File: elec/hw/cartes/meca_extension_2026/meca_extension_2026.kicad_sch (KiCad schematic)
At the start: 101 parts, among them J1 2-1445051-3, J14 22272031, J15 22272031, J16 5264-3P, J26 22053051, J27 22053041, Q19 BSS84, Q20 2N7002, U1 TCA9548APWR, U11 LV14340DDAR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

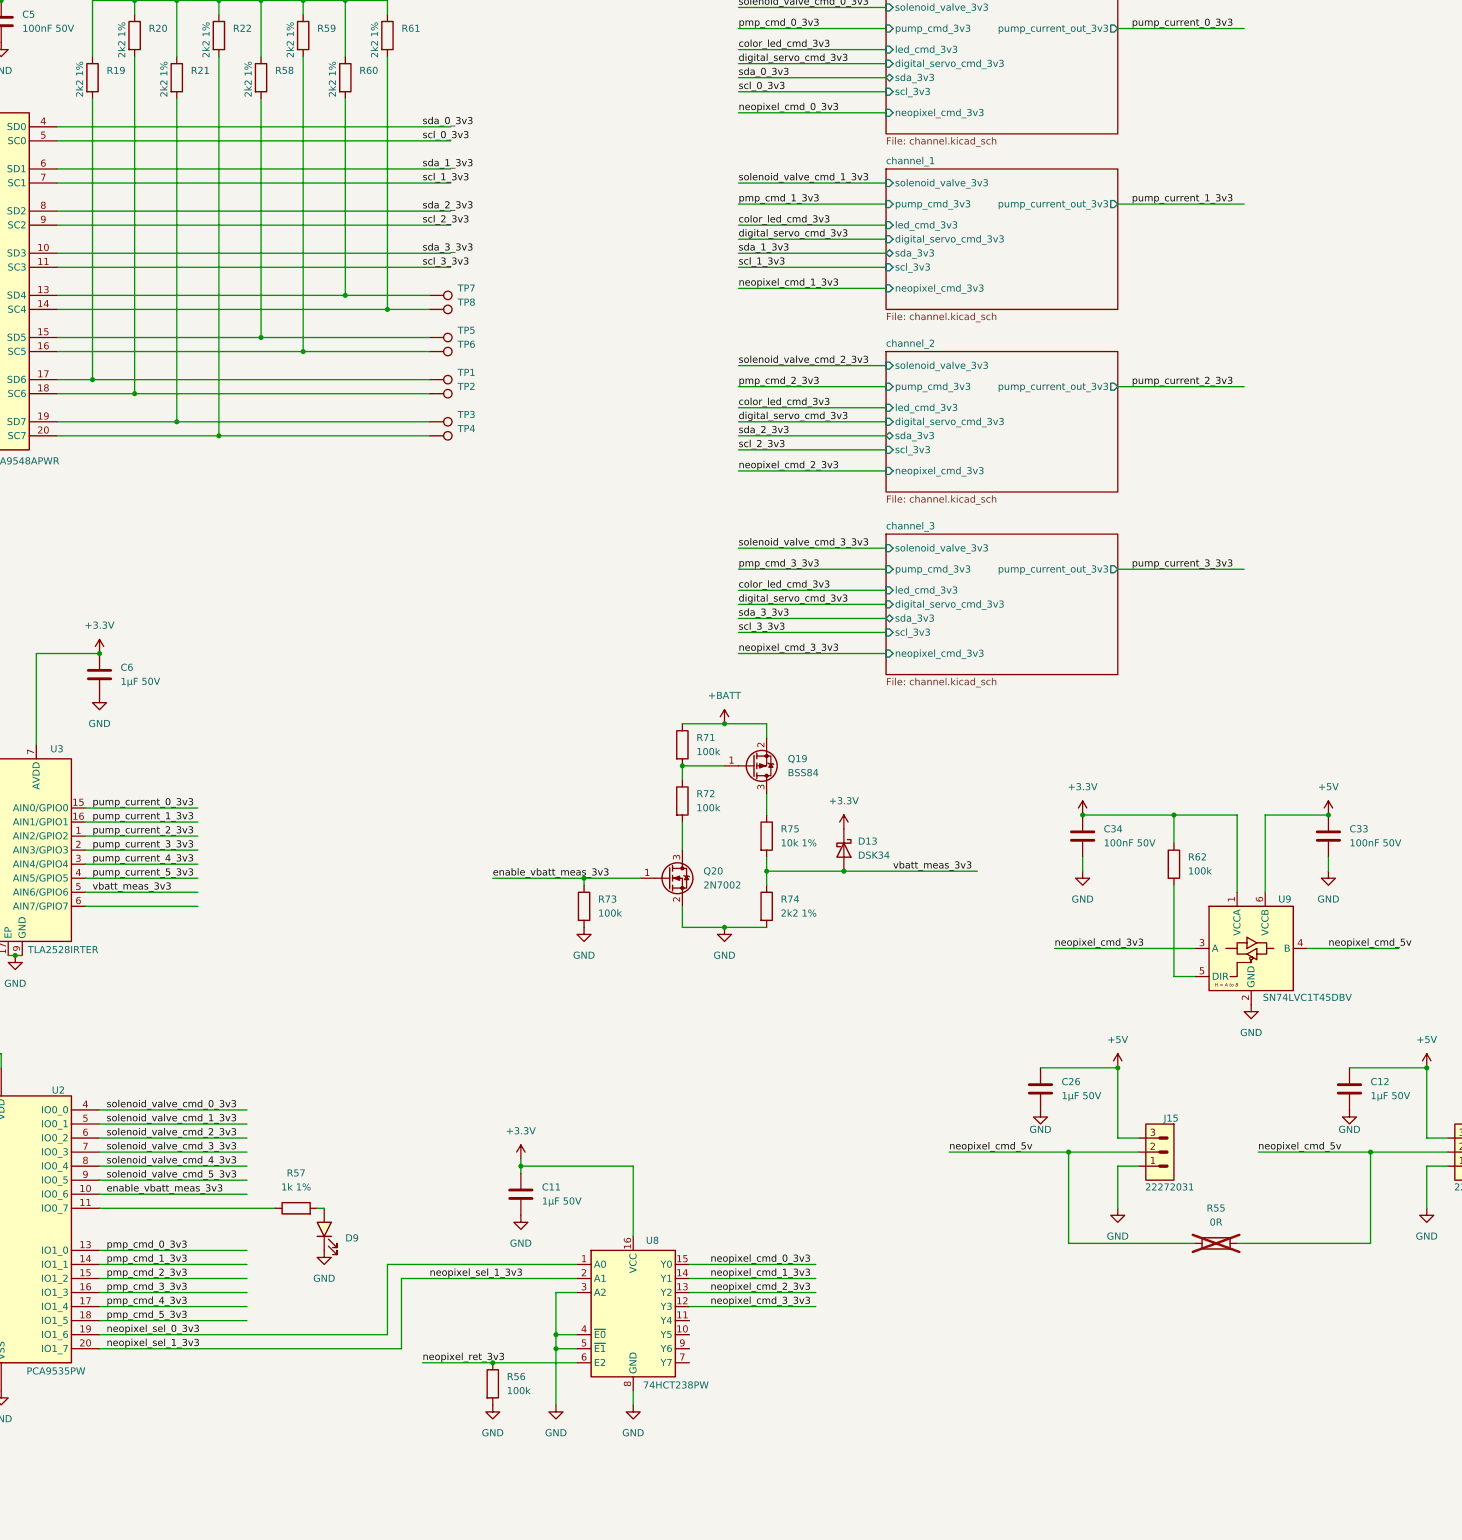
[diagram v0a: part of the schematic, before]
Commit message: meca_extension : schematic correction and routing modified accordingly
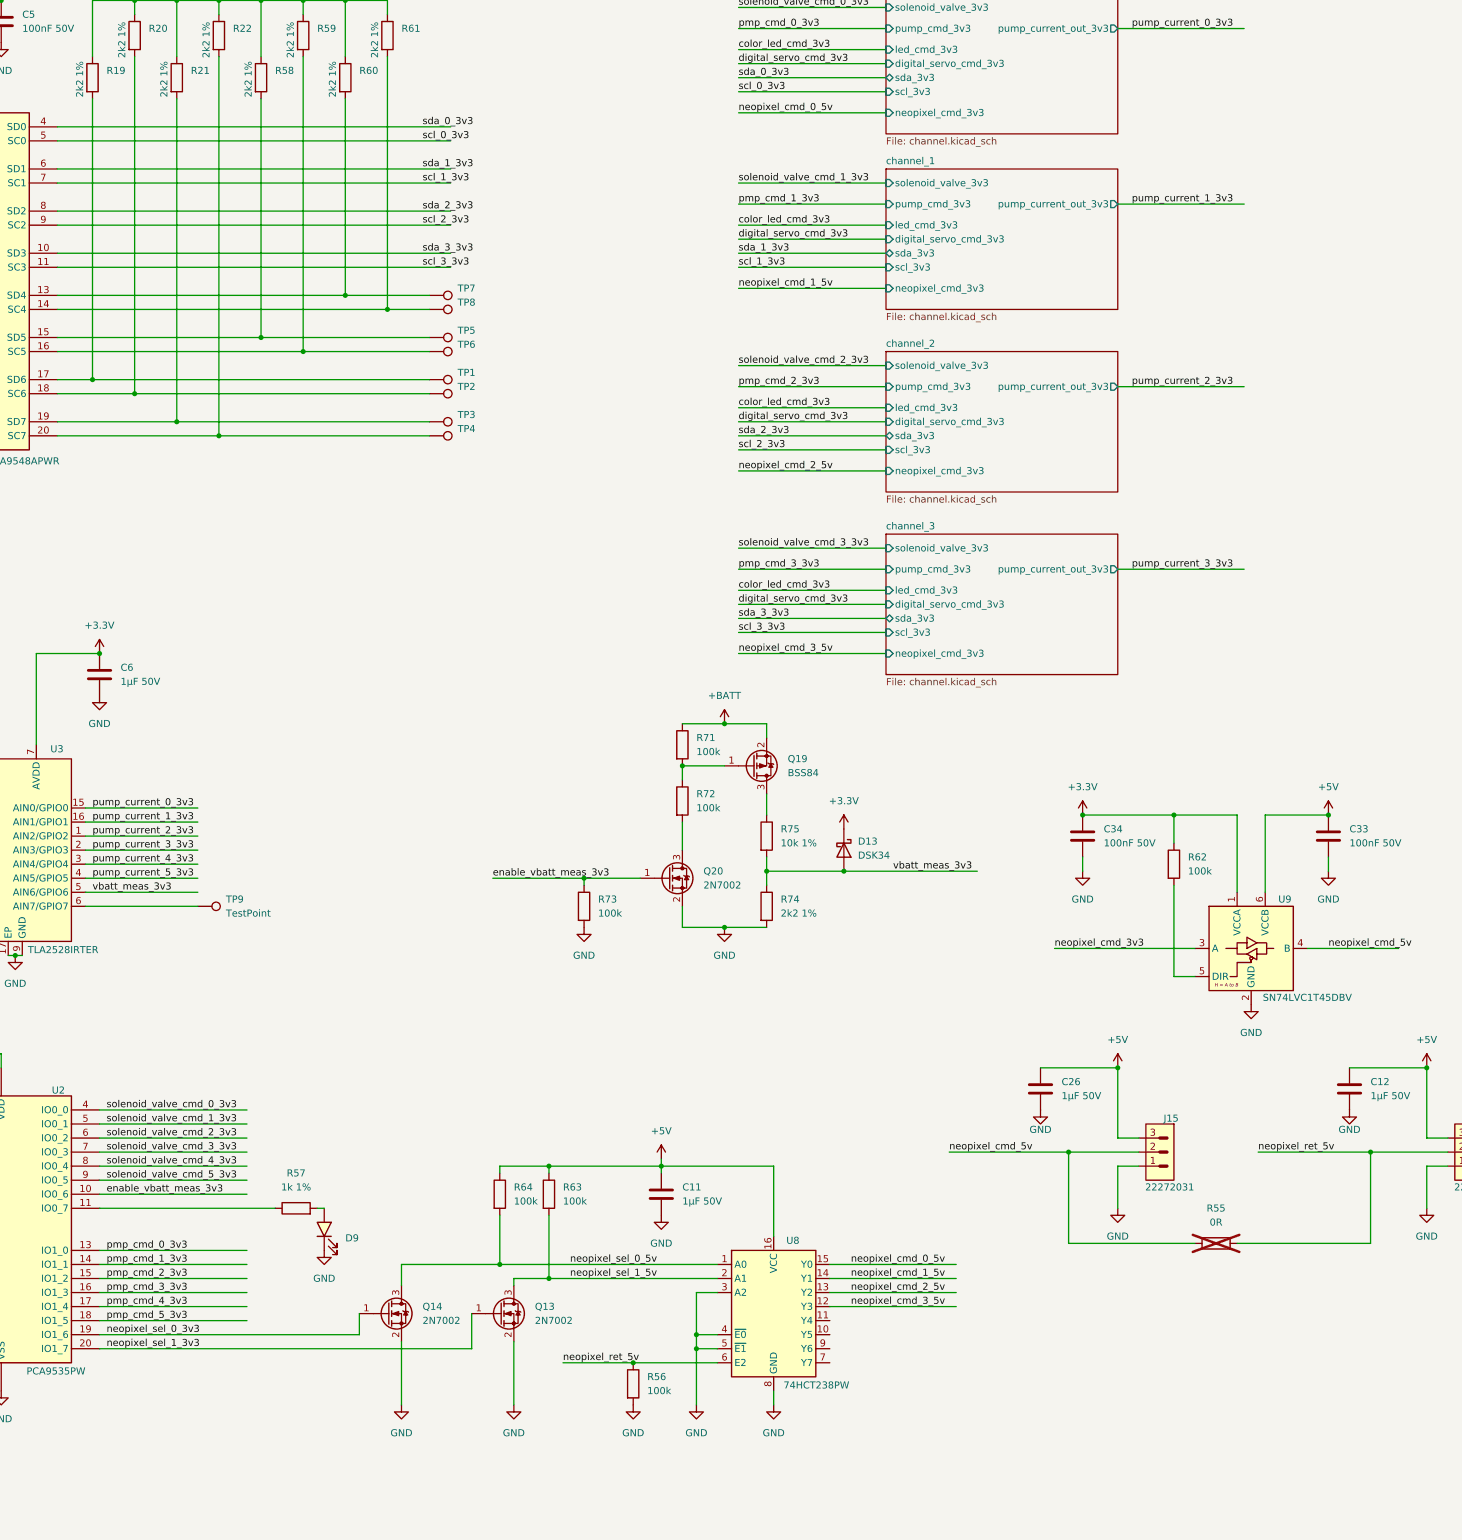
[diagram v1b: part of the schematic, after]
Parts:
- added Q13, Q14: 2N7002, cocotter_transistors:SOT-23-3, symbol cocotter_transistors:2N7002
- added R63, R64: 100k, cocotter_resistor:r0603_reflow, symbol cocotter_resistors:R_100k_0603_1%
- added TP9: TestPoint, cocotter_others:testpoint-THT-0.8mm, symbol cocotter_others:TestPoint_0.8mm
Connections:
- net +3.3V: no longer C11.1, U8.16 (VCC)
- net +5V: now also C11.1, U8.16 (VCC), R63.1, R64.1
- net GND: now also Q13.2 (S), Q14.2 (S)
- net neopixel_cmd_5v: no longer J14.2, R55.2
- net neopixel_sel_0_3v3: now also Q14.1 (G); no longer U8.1 (A0)
- net at U3.6 (AIN7/GPIO7): now also TP9.1
- net at U2.20 (IO1_7): now also Q13.1 (G); no longer U8.2 (A1)
- net neopixel_cmd_0_3v3 renamed neopixel_cmd_0_5v
- net neopixel_cmd_1_3v3 renamed neopixel_cmd_1_5v
- net neopixel_cmd_2_3v3 renamed neopixel_cmd_2_5v
- net neopixel_cmd_3_3v3 renamed neopixel_cmd_3_5v
- net neopixel_ret_3v3 renamed neopixel_ret_5v
- net neopixel_ret_5v: now also J14.2, R55.2
- new net neopixel_sel_0_5v: Q14.3 (D), R64.2, U8.1 (A0)
- new net neopixel_sel_1_5v: Q13.3 (D), R63.2, U8.2 (A1)
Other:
- moved on the sheet: C11, R56, U8

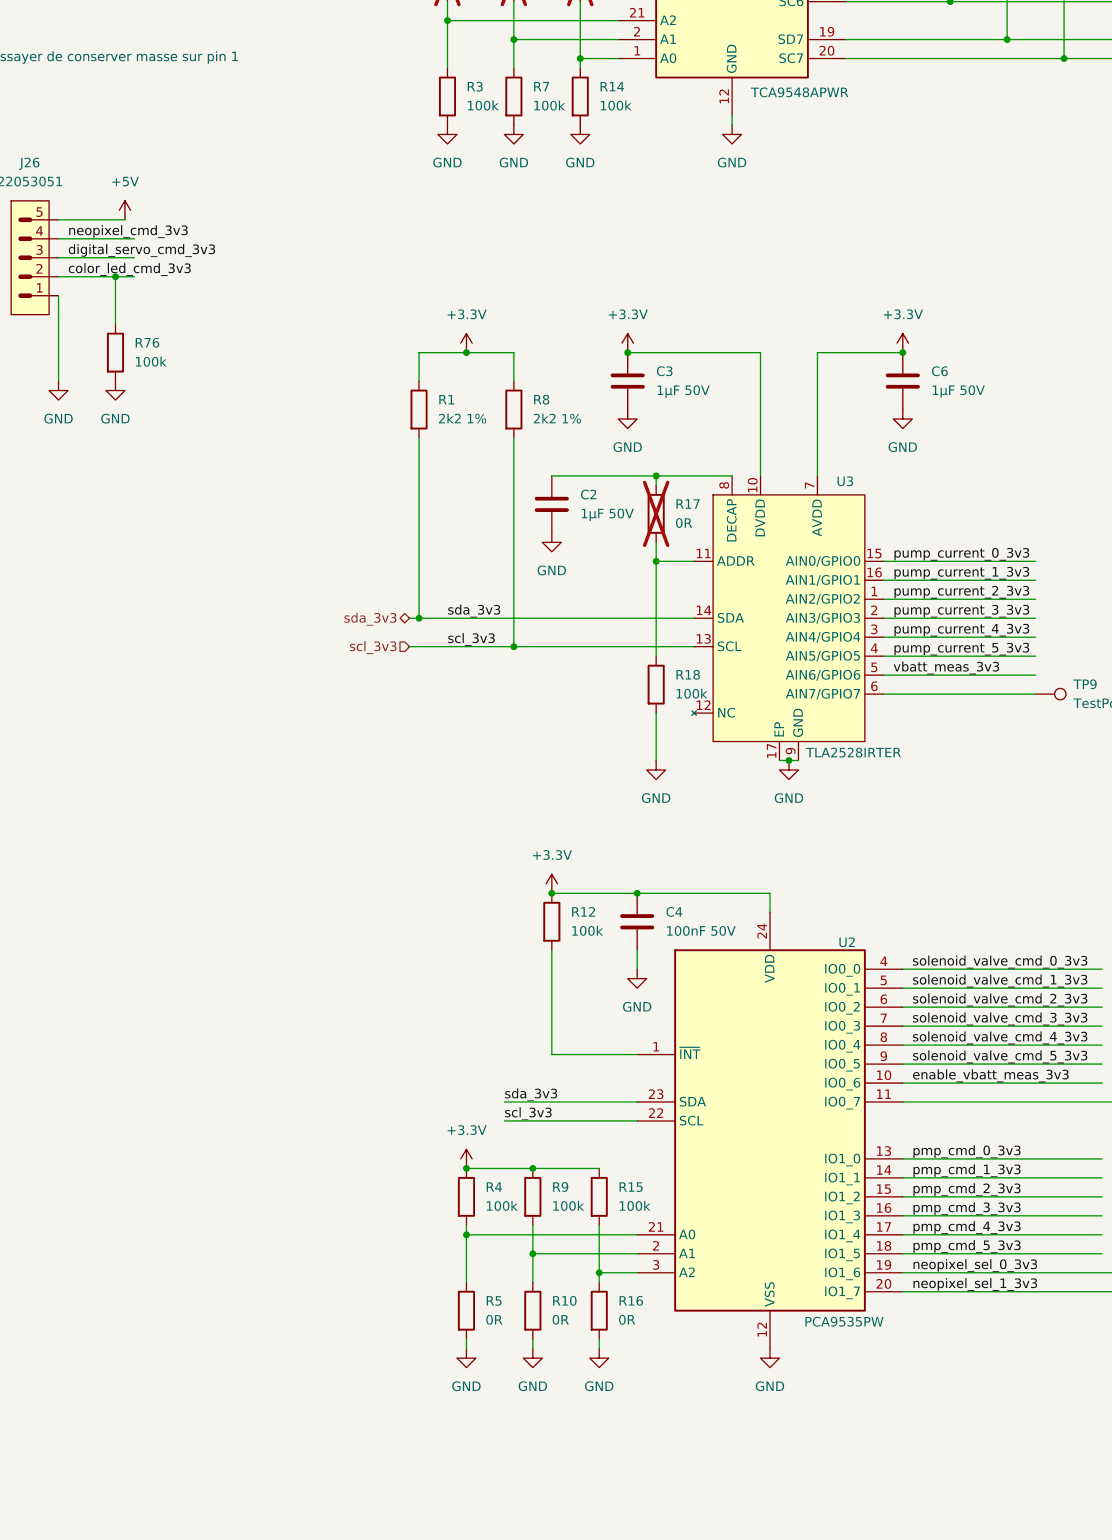
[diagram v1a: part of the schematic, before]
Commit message: meca extension: silkscreen modified, led moved
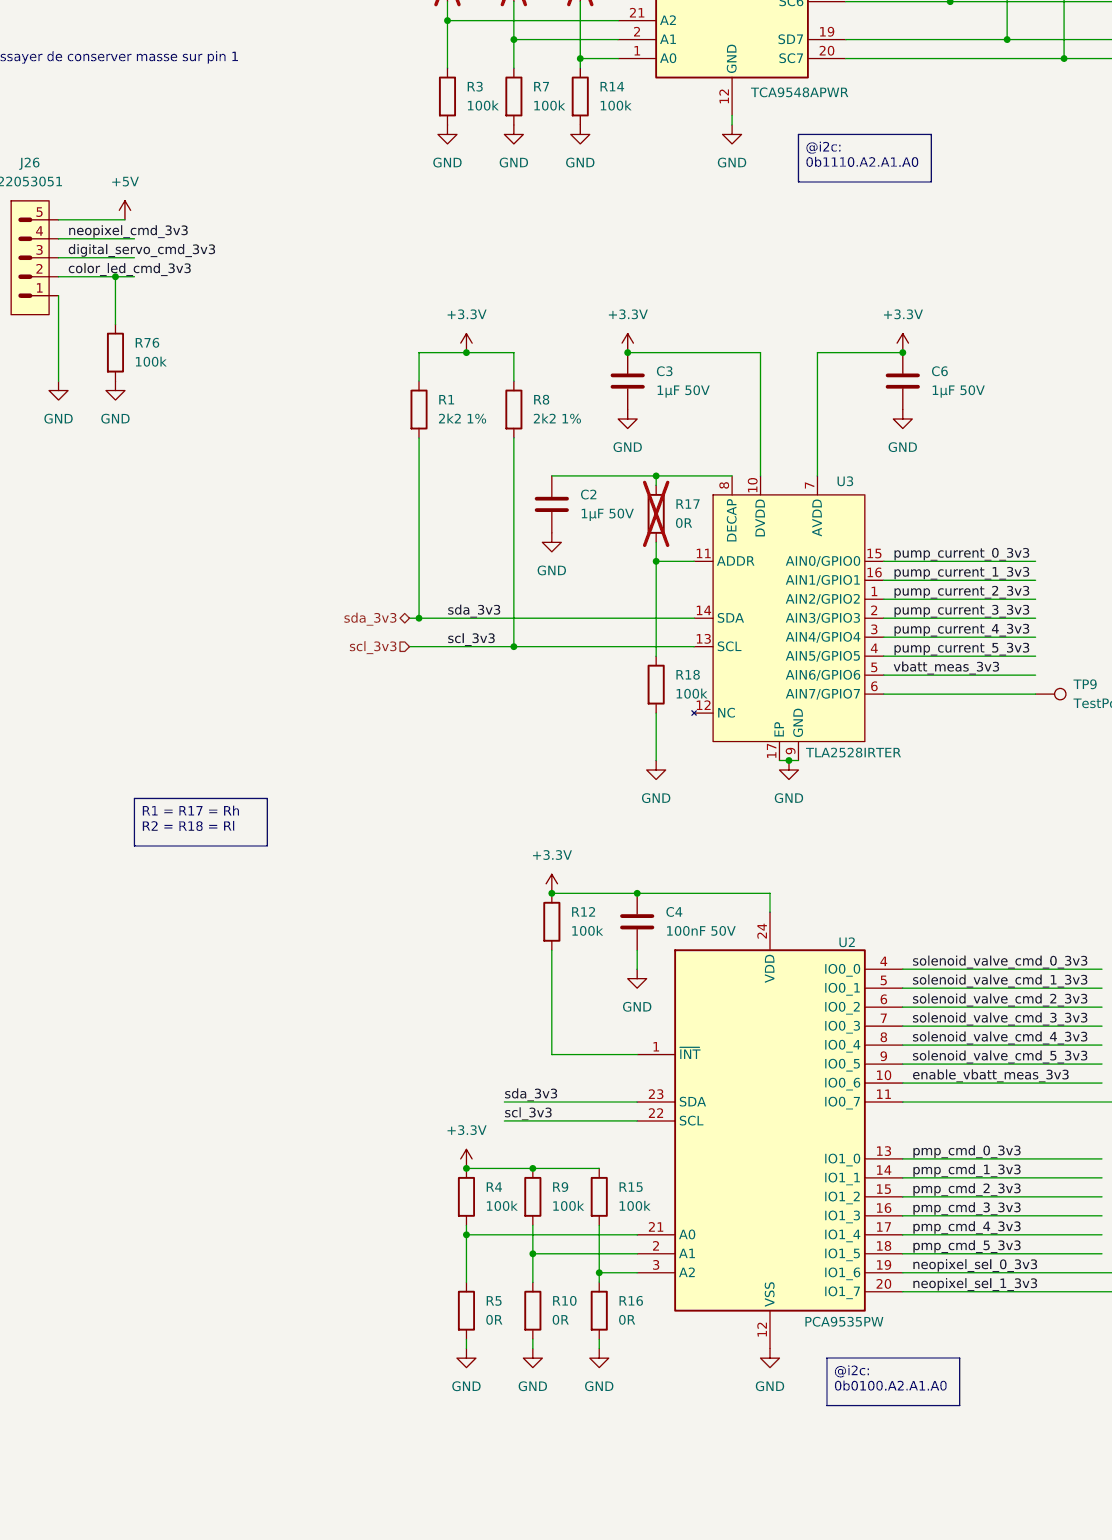
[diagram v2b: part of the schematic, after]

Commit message: meca_extension : led command can be 3v3 or 5v, selecion resistors added
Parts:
- added R65, R66: 0R, cocotter_resistor:r0603_reflow, symbol cocotter_resistors:R_0R_0603
- C33, C34, R62, U9: now not fitted
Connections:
- net neopixel_cmd_5v: now also R65.2, R66.2; no longer U9.4 (B)
- net neopixel_cmd_3v3 renamed neopixel_cmd_con
- net neopixel_cmd_con: now also R66.1
- new net: R65.1, U9.4 (B)
